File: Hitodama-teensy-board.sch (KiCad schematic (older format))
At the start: 16 parts, among them J1 Jack-DC, J2 Conn_01x20_Female, J3 Conn_01x20_Female, J4 Conn_01x20_Female, U4 Teensy3.6

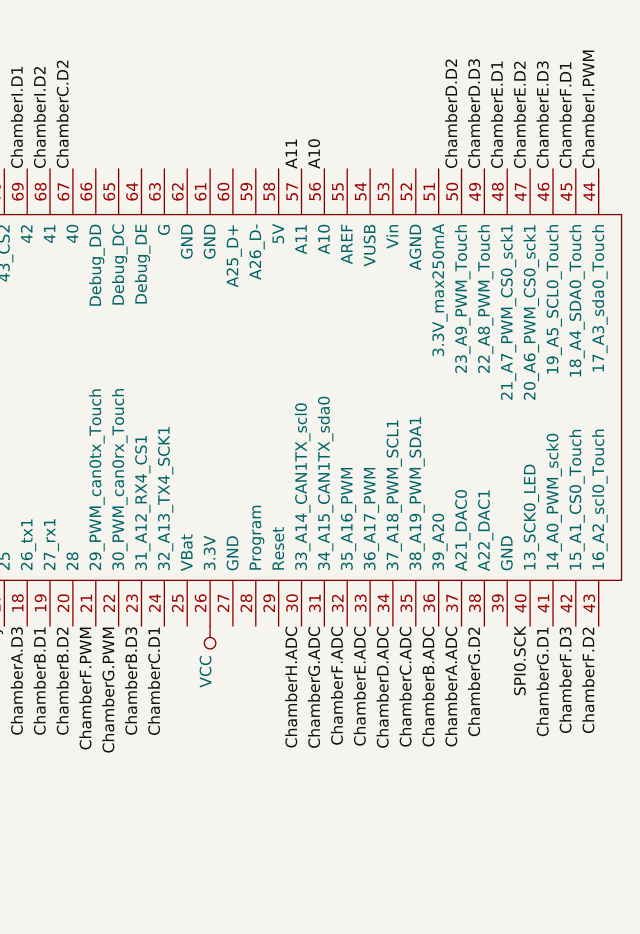
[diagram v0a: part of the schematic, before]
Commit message: fix wrong adc pins in teensy board
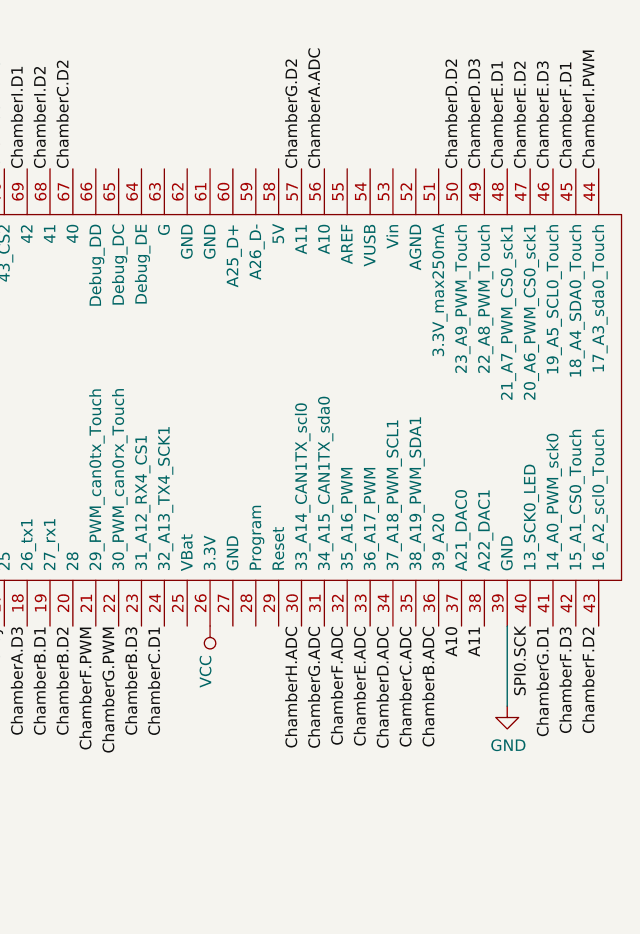
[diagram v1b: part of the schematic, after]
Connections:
- wire segments 0 -> 1
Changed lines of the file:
@@
 Text Label 9600 3600 3    50   ~ 0
 ChamberF.D2
-Text Label 9100 3600 3    50   ~ 0
+Text Label 8300 1600 1    50   ~ 0
 ChamberG.D2
 Text Label 6900 1600 1    50   ~ 0
@@
 Text Label 7000 1600 1    50   ~ 0
 ChamberH.D3
-Text Label 9000 3600 3    50   ~ 0
+Text Label 8400 1600 1    50   ~ 0
 ChamberA.ADC
 Text Label 8900 3600 3    50   ~ 0
@@
 Text Label 6200 1600 1    50   ~ 0
 ChamberI.ADC
-Text Label 8300 1600 1    50   ~ 0
+Text Label 9100 3600 3    50   ~ 0
 A11
-Text Label 8400 1600 1    50   ~ 0
+Text Label 9000 3600 3    50   ~ 0
 A10
 Text Label 5400 1600 1    50   ~ 0
@@
 	-1   0    0    1
 $EndComp
+$Comp
+L power:GND #PWR?
+U 1 1 5CF41CA3
+P 9200 3950
+F 0 "#PWR?" H 9200 3700 50  0001 C CNN
+F 1 "GND" H 9205 3777 50  0000 C CNN
+F 2 "" H 9200 3950 50  0001 C CNN
+F 3 "" H 9200 3950 50  0001 C CNN
+	1    9200 3950
+	1    0    0    -1
+$EndComp
+Wire Wire Line
+	9200 3950 9200 3600
 $EndSCHEMATC

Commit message: Merge branch 'joaquin' into HEAD
# Conflicts:
#	Hitodama-teensy-board.kicad_pcb
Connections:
- wire segments 1 -> 2
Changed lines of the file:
@@
 Wire Wire Line
 	9200 3950 9200 3600
+$Comp
+L power:VCC #PWR?
+U 1 1 5CF42C33
+P 8900 1450
+F 0 "#PWR?" H 8900 1300 50  0001 C CNN
+F 1 "VCC" V 8918 1577 50  0000 L CNN
+F 2 "" H 8900 1450 50  0001 C CNN
+F 3 "" H 8900 1450 50  0001 C CNN
+	1    8900 1450
+	0    -1   -1   0
+$EndComp
+Wire Wire Line
+	8900 1450 8900 1600
 $EndSCHEMATC
